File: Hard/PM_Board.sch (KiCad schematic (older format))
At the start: 64 parts, among them J1 Micro_SD_Card_Det_Hirose_DM3AT, J101 LiPo_V+, J102 LiPo_V-, J2 KRC_Conn_SWD, J3 USB_B_Micro, J4 KRC_Conn_CAN, J5 KRC_Conn_CAN, J6 KRC_Conn_CAN, Q1 SSM6J501NU, Q2 2n7002, U1 CY8C58xxLTI-LPxxx, U2 INA226, U3 NCV7342, Y1 24MHz

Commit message: [add] 逆流防止用ダイオードを追加
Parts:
- added D6, D7: RSX101VA, Diode_SMD:D_TUMD2, symbol Device:D_Schottky_Small
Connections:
- net +3V3: now also D7.2 (A)
- net +5V: now also D6.2 (A)
- net at C17.1, C19.1, Q1.4 (S)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: now also D6.1 (K), D7.1 (K)
- no-connect marks 9 -> 36
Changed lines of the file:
@@
 EESchema Schematic File Version 4
 LIBS:PM_Board-cache
-EELAYER 26 0
+EELAYER 30 0
 EELAYER END
 $Descr A4 11693 8268
@@
 P 2900 2950
 F 0 "#PWR0133" H 2900 2700 50  0001 C CNN
-F 1 "GND" H 2905 2777 50  0000 C CNN
+F 1 "GND" H 3050 2900 50  0000 C CNN
 F 2 "" H 2900 2950 50  0001 C CNN
 F 3 "" H 2900 2950 50  0001 C CNN
@@
 U 1 1 5DC30610
 P 2900 4550
-F 0 "VR2" H 2900 4865 50  0000 C CNN
-F 1 "NCP718ASN330T1G" H 2900 4774 50  0000 C CNN
+F 0 "VR2" H 2900 4650 50  0000 C CNN
+F 1 "NCP718ASN330T1G" H 3300 4350 50  0000 C CNN
 F 2 "Package_TO_SOT_SMD:TSOT-23-5" H 2800 4750 50  0001 C CNN
 F 3 "https://www.onsemi.com/pub/Collateral/NCP718-D.PDF" H 2900 4850 50  0001 C CNN
@@
 U 1 1 5DC3080F
 P 2900 3550
-F 0 "VR1" H 2900 3865 50  0000 C CNN
-F 1 "NCP718ASN500T1G" H 2900 3774 50  0000 C CNN
+F 0 "VR1" H 2900 3650 50  0000 C CNN
+F 1 "NCP718ASN500T1G" H 3300 3350 50  0000 C CNN
 F 2 "Package_TO_SOT_SMD:TSOT-23-5" H 2800 3750 50  0001 C CNN
 F 3 "https://www.onsemi.com/pub/Collateral/NCP718-D.PDF" H 2900 3850 50  0001 C CNN
@@
 $EndComp
 Wire Wire Line
-	2400 3500 2550 3500
+	2400 3500 2450 3500
 Wire Wire Line
 	2400 3600 2550 3600
@@
 Connection ~ 2400 4500
 Wire Wire Line
-	2400 4500 2550 4500
-Wire Wire Line
-	3250 4500 3700 4500
-Wire Wire Line
-	3250 3500 3700 3500
+	2400 4500 2450 4500
+Wire Wire Line
+	3250 4500 3350 4500
+Wire Wire Line
+	3250 3500 3350 3500
 Wire Wire Line
 	2900 3800 2900 3900
@@
 Wire Wire Line
 	5050 4100 5350 4100
+$Comp
+L Device:D_Schottky_Small D6
+U 1 1 5D91C8E7
+P 2900 3350
+F 0 "D6" H 2900 3555 50  0000 C CNN
+F 1 "RSX101VA" H 2900 3464 50  0000 C CNN
+F 2 "Diode_SMD:D_TUMD2" V 2900 3350 50  0001 C CNN
+F 3 "http://akizukidenshi.com/download/ds/rohm/rsx101vam30-j.pdf" V 2900 3350 50  0001 C CNN
+F 4 "秋月電子" H 2900 3350 50  0001 C CNN "Agency"
+F 5 "http://akizukidenshi.com/catalog/g/gI-05951/" H 2900 3350 50  0001 C CNN "Link"
+F 6 "RSX101VAM-30TR" H 2900 3350 50  0001 C CNN "MPN"
+	1    2900 3350
+	1    0    0    -1
+$EndComp
+Wire Wire Line
+	2800 3350 2450 3350
+Wire Wire Line
+	2450 3350 2450 3500
+Connection ~ 2450 3500
+Wire Wire Line
+	2450 3500 2550 3500
+Wire Wire Line
+	3000 3350 3350 3350
+Wire Wire Line
+	3350 3350 3350 3500
+Connection ~ 3350 3500
+Wire Wire Line
+	3350 3500 3700 3500
+$Comp
+L Device:D_Schottky_Small D7
+U 1 1 5D94B0D3
+P 2900 4350
+F 0 "D7" H 2900 4555 50  0000 C CNN
+F 1 "RSX101VA" H 2900 4464 50  0000 C CNN
+F 2 "Diode_SMD:D_TUMD2" V 2900 4350 50  0001 C CNN
+F 3 "http://akizukidenshi.com/download/ds/rohm/rsx101vam30-j.pdf" V 2900 4350 50  0001 C CNN
+F 4 "秋月電子" H 2900 4350 50  0001 C CNN "Agency"
+F 5 "http://akizukidenshi.com/catalog/g/gI-05951/" H 2900 4350 50  0001 C CNN "Link"
+F 6 "RSX101VAM-30TR" H 2900 4350 50  0001 C CNN "MPN"
+	1    2900 4350
+	1    0    0    -1
+$EndComp
+Wire Wire Line
+	2800 4350 2450 4350
+Wire Wire Line
+	2450 4350 2450 4500
+Connection ~ 2450 4500
+Wire Wire Line
+	2450 4500 2550 4500
+Wire Wire Line
+	3000 4350 3350 4350
+Wire Wire Line
+	3350 4350 3350 4500
+Connection ~ 3350 4500
+Wire Wire Line
+	3350 4500 3700 4500
+NoConn ~ 5350 3200
+NoConn ~ 5350 3300
+NoConn ~ 5350 3400
+NoConn ~ 5350 3500
+NoConn ~ 5350 4500
+NoConn ~ 5350 4600
+NoConn ~ 5350 4850
+NoConn ~ 5350 4950
+NoConn ~ 5350 5050
+NoConn ~ 5350 5150
+NoConn ~ 5350 5250
+NoConn ~ 8050 2800
+NoConn ~ 8050 2900
+NoConn ~ 8050 3000
+NoConn ~ 8050 3100
+NoConn ~ 8050 3200
+NoConn ~ 8050 3300
+NoConn ~ 8050 3700
+NoConn ~ 8050 3800
+NoConn ~ 8050 3900
+NoConn ~ 8050 4000
+NoConn ~ 8050 4100
+NoConn ~ 8050 4200
+NoConn ~ 8050 4300
+NoConn ~ 8050 4400
+NoConn ~ 8050 5200
+NoConn ~ 8050 5300
 $EndSCHEMATC

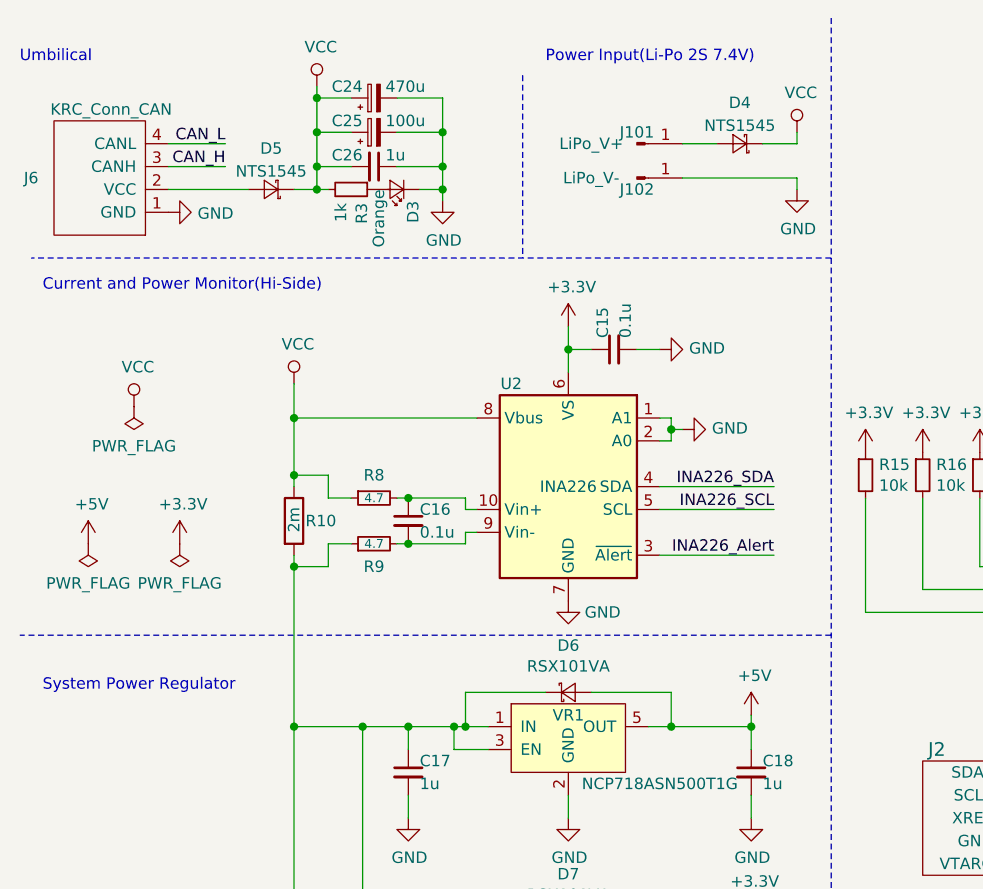
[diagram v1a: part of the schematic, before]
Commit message: [update] パターンを編集完了
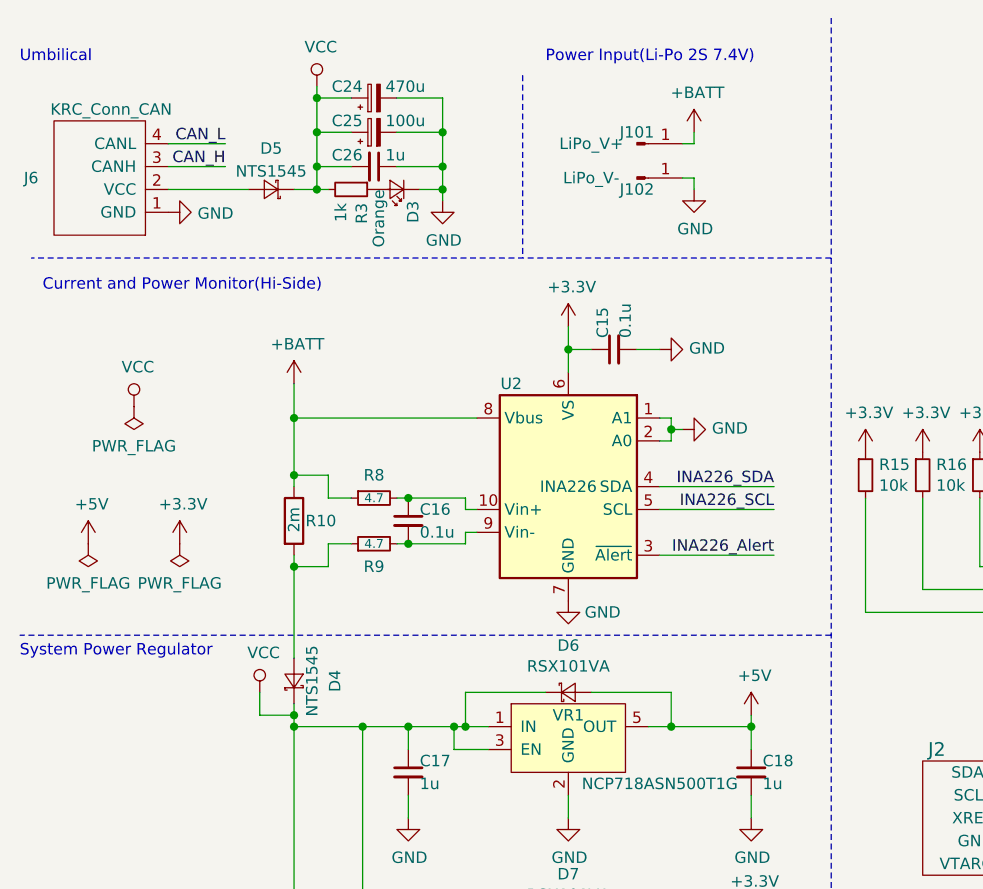
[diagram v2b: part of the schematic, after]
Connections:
- net VCC: now also C17.1, C19.1, D6.1 (K), D7.1 (K), Q1.4 (S), Q1.8, R13.1, VR1.1 (IN), VR1.3 (EN), VR2.1 (IN), VR2.3 (EN); no longer R10.1, R8.1, U2.8 (Vbus)
- net at D4.2 (A): now also R10.2, R9.1; no longer J101.1 (Pin_1)
- new net +BATT: J101.1 (Pin_1), R10.1, R8.1, U2.8 (Vbus)
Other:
- moved on the sheet: D4
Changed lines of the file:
@@
 L power:GND #PWR0134
 U 1 1 5DCE33BD
-P 3900 1150
-F 0 "#PWR0134" H 3900 900 50  0001 C CNN
-F 1 "GND" H 3905 977 50  0000 C CNN
-F 2 "" H 3900 1150 50  0001 C CNN
-F 3 "" H 3900 1150 50  0001 C CNN
-	1    3900 1150
+P 3450 1150
+F 0 "#PWR0134" H 3450 900 50  0001 C CNN
+F 1 "GND" H 3455 977 50  0000 C CNN
+F 2 "" H 3450 1150 50  0001 C CNN
+F 3 "" H 3450 1150 50  0001 C CNN
+	1    3450 1150
 	1    0    0    -1
 $EndComp
@@
 Text Notes 600  1600 0    50   ~ 0
 Current and Power Monitor(Hi-Side)
-Text Notes 600  3350 0    50   ~ 0
+Text Notes 500  3200 0    50   ~ 0
 System Power Regulator
 Text Notes 750  5350 0    50   ~ 0
@@
 	0    -1   1    0
 $EndComp
-$Comp
-L power:VCC #PWR0141
-U 1 1 5DAE3A9E
-P 3900 900
-F 0 "#PWR0141" H 3900 750 50  0001 C CNN
-F 1 "VCC" H 3917 1073 50  0000 C CNN
-F 2 "" H 3900 900 50  0001 C CNN
-F 3 "" H 3900 900 50  0001 C CNN
-	1    3900 900
-	1    0    0    -1
-$EndComp
-Wire Wire Line
-	3900 900  3900 950
-$Comp
-L power:VCC #PWR0142
-U 1 1 5DB04A5B
-P 1700 2000
-F 0 "#PWR0142" H 1700 1850 50  0001 C CNN
-F 1 "VCC" H 1717 2173 50  0000 C CNN
-F 2 "" H 1700 2000 50  0001 C CNN
-F 3 "" H 1700 2000 50  0001 C CNN
-	1    1700 2000
-	1    0    0    -1
-$EndComp
 Wire Wire Line
 	1700 2000 1700 2150
@@
 L Device:D_Schottky_Small D4
 U 1 1 5DD308E3
-P 3650 950
-F 0 "D4" H 3650 800 50  0000 C TNN
-F 1 "NTS1545" H 3650 900 50  0000 C TNN
-F 2 "KUTKiCad_footprint:DFN5_5x6_1.27P" H 3650 950 50  0001 C CNN
-F 3 "https://www.onsemi.com/pub/Collateral/NTS1545MFS-D.PDF" H 3650 950 50  0001 C CNN
-F 4 "Digikey" H 3650 950 50  0001 C CNN "Agency"
-F 5 "NTS1545MFST1G" H 3650 950 50  0001 C CNN "MPN"
-F 6 "https://www.digikey.jp/product-detail/ja/on-semiconductor/NTS1545MFST1G/NTS1545MFST1GOSCT-ND/5022596" H 3650 950 50  0001 C CNN "Link"
-	1    3650 950
-	-1   0    0    1
+P 1700 3300
+F 0 "D4" H 1700 3150 50  0000 C TNN
+F 1 "NTS1545" H 1700 3250 50  0000 C TNN
+F 2 "KUTKiCad_footprint:DFN5_5x6_1.27P" H 1700 3300 50  0001 C CNN
+F 3 "https://www.onsemi.com/pub/Collateral/NTS1545MFS-D.PDF" H 1700 3300 50  0001 C CNN
+F 4 "Digikey" H 1700 3300 50  0001 C CNN "Agency"
+F 5 "NTS1545MFST1G" H 1700 3300 50  0001 C CNN "MPN"
+F 6 "https://www.digikey.jp/product-detail/ja/on-semiconductor/NTS1545MFST1G/NTS1545MFST1GOSCT-ND/5022596" H 1700 3300 50  0001 C CNN "Link"
+	1    1700 3300
+	0    -1   -1   0
 $EndComp
 $Comp
@@
 	8750 3500 8750 3600
 Wire Wire Line
-	1700 2800 1700 3500
-Connection ~ 1700 2800
-Wire Wire Line
 	1400 950  1150 950
 Wire Wire Line
-	3750 950  3900 950
-Wire Wire Line
-	3900 1150 3900 1100
+	3450 1150 3450 1100
 $Comp
 L Device:LED_Small D3
@@
 Wire Wire Line
 	2350 1150 2350 1200
-Wire Wire Line
-	3550 950  3400 950
-Wire Wire Line
-	3900 1100 3400 1100
 $Comp
 L Device:R_Small R15
@@
 Wire Wire Line
 	2850 5650 3250 5650
-Wire Wire Line
-	1700 3500 1700 5150
-Connection ~ 1700 3500
 Wire Wire Line
 	1700 5850 1700 6150
@@
 NoConn ~ 8050 5200
 NoConn ~ 8050 5300
+$Comp
+L power:+BATT #PWR0141
+U 1 1 5DC0E776
+P 3450 900
+F 0 "#PWR0141" H 3450 750 50  0001 C CNN
+F 1 "+BATT" H 3465 1073 50  0000 C CNN
+F 2 "" H 3450 900 50  0001 C CNN
+F 3 "" H 3450 900 50  0001 C CNN
+	1    3450 900
+	1    0    0    -1
+$EndComp
+Wire Wire Line
+	3450 900  3450 950
+Wire Wire Line
+	3450 950  3400 950
+$Comp
+L power:+BATT #PWR0142
+U 1 1 5DC26E97
+P 1700 2000
+F 0 "#PWR0142" H 1700 1850 50  0001 C CNN
+F 1 "+BATT" H 1715 2173 50  0000 C CNN
+F 2 "" H 1700 2000 50  0001 C CNN
+F 3 "" H 1700 2000 50  0001 C CNN
+	1    1700 2000
+	1    0    0    -1
+$EndComp
+Wire Wire Line
+	1700 2800 1700 3200
+Connection ~ 1700 2800
+Wire Wire Line
+	1700 3400 1700 3450
+Connection ~ 1700 3500
+Wire Wire Line
+	3450 1100 3400 1100
+Wire Wire Line
+	1700 3500 1700 5150
+$Comp
+L power:VCC #PWR0151
+U 1 1 5DD8F5B1
+P 1550 3350
+F 0 "#PWR0151" H 1550 3200 50  0001 C CNN
+F 1 "VCC" H 1567 3523 50  0000 C CNN
+F 2 "" H 1550 3350 50  0001 C CNN
+F 3 "" H 1550 3350 50  0001 C CNN
+	1    1550 3350
+	1    0    0    -1
+$EndComp
+Wire Wire Line
+	1550 3350 1550 3450
+Wire Wire Line
+	1550 3450 1700 3450
+Connection ~ 1700 3450
+Wire Wire Line
+	1700 3450 1700 3500
 $EndSCHEMATC

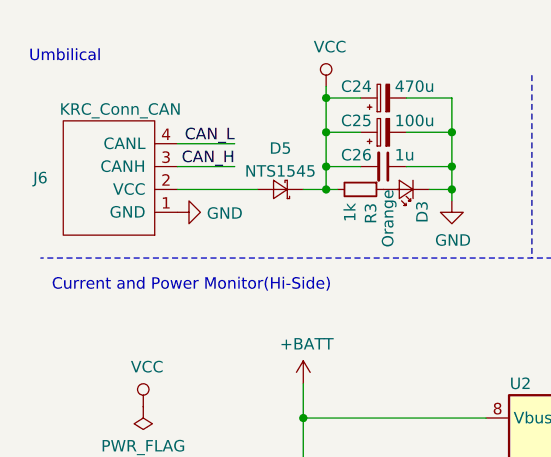
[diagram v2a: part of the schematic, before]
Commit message: [update] アンビリカルをDF1Eに変更
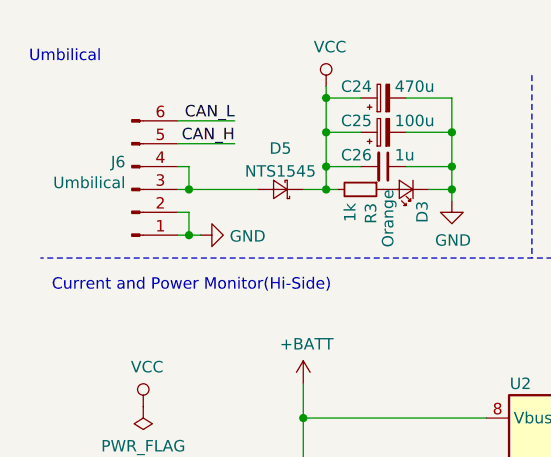
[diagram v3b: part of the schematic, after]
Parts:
- removed J6: KRC_Conn_CAN, KUTKiCad_footprint:Hirose_DF33-DF33C-4DP-3.3DSA_2x02_P3.3_Vertical, symbol KUTKiCad_symbol:KRC_Conn_CAN
- added J6: Umbilical, KUTKiCad_footprint:Hirose_DF1E_DF1E-6P-2.5DS_1x06_P2.5mm_Vertical, symbol Connector:Conn_01x06_Male
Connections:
- net CAN_H: now also J6.5 (Pin_5)
- net CAN_L: now also J6.6 (Pin_6)
- net GND: now also J6.1 (Pin_1), J6.2 (Pin_2)
- net at D5.2 (A): now also J6.3 (Pin_3), J6.4 (Pin_4)
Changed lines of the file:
@@
 EESchema Schematic File Version 4
 LIBS:PM_Board-cache
-EELAYER 30 0
+EELAYER 26 0
 EELAYER END
 $Descr A4 11693 8268
@@
 microSD
 Connection ~ 2000 3500
-$Comp
-L KUTKiCad_symbol:KRC_Conn_CAN J6
-U 1 1 5D97F500
-P 1050 1100
-F 0 "J6" H 1550 1100 50  0000 C CNN
-F 1 "KRC_Conn_CAN" H 1200 800 50  0000 C CNN
-F 2 "KUTKiCad_footprint:Hirose_DF33-DF33C-4DP-3.3DSA_2x02_P3.3_Vertical" H 1050 1100 50  0001 C CNN
-F 3 "https://www.hirose.com/product/document?clcode=&productname=&series=DF33C&documenttype=Catalog&lang=ja&documentid=D51103_ja" H 1050 1100 50  0001 C CNN
-F 4 "Digikey" H 1050 1100 50  0001 C CNN "Agency"
-F 5 "DF33C-4DP-3.3DSA(24)" H 1050 1100 50  0001 C CNN "MPN"
-F 6 "https://www.digikey.jp/products/ja?keywords=DF33C-4DP-3.3DSA(24)" H 0   0   50  0001 C CNN "Link"
-	1    1050 1100
-	-1   0    0    1
-$EndComp
 Text Label 1750 7000 2    50   ~ 0
 CAN_H
 Text Label 1750 7100 2    50   ~ 0
 CAN_L
-Text Label 1400 1050 2    50   ~ 0
+Text Label 1400 950  2    50   ~ 0
 CAN_H
-Text Label 1400 950  2    50   ~ 0
+Text Label 1400 850  2    50   ~ 0
 CAN_L
 Wire Wire Line
-	1400 1050 1150 1050
+	1400 950  1150 950
 $Comp
 L power:GND #PWR0140
 U 1 1 5DA52B7A
-P 1150 1250
-F 0 "#PWR0140" H 1150 1000 50  0001 C CNN
-F 1 "GND" V 1155 1122 50  0000 R CNN
-F 2 "" H 1150 1250 50  0001 C CNN
-F 3 "" H 1150 1250 50  0001 C CNN
-	1    1150 1250
+P 1250 1350
+F 0 "#PWR0140" H 1250 1100 50  0001 C CNN
+F 1 "GND" V 1255 1222 50  0000 R CNN
+F 2 "" H 1250 1350 50  0001 C CNN
+F 3 "" H 1250 1350 50  0001 C CNN
+	1    1250 1350
 	0    -1   1    0
 $EndComp
@@
 	8750 3500 8750 3600
 Wire Wire Line
-	1400 950  1150 950
+	1400 850  1150 850
 Wire Wire Line
 	3450 1150 3450 1100
@@
 Connection ~ 1800 1150
 Wire Wire Line
-	1500 1150 1150 1150
+	1500 1150 1200 1150
 $Comp
 L KUTKiCad_symbol:SSM6J501NU Q1
@@
 Wire Wire Line
 	1700 3450 1700 3500
+$Comp
+L Connector:Conn_01x06_Male J6
+U 1 1 5D968A87
+P 950 1150
+F 0 "J6" H 922 1030 50  0000 R CNN
+F 1 "Umbilical" H 922 1121 50  0000 R CNN
+F 2 "KUTKiCad_footprint:Hirose_DF1E_DF1E-6P-2.5DS_1x06_P2.5mm_Vertical" H 950 1150 50  0001 C CNN
+F 3 "https://www.hirose.com/product/document?clcode=&productname=&series=DF1E&documenttype=Catalog&lang=ja&documentid=D49651_ja" H 950 1150 50  0001 C CNN
+F 4 "Digikey" H 950 1150 50  0001 C CNN "Agency"
+F 5 "DF1EC-6P-2.5DSA(35)" H 950 1150 50  0001 C CNN "MPN"
+F 6 "https://www.digikey.jp/product-detail/ja/hirose-electric-co-ltd/DF1EC-6P-2.5DSA-35/H125168-ND/5416404" H 950 1150 50  0001 C CNN "Link"
+	1    950  1150
+	1    0    0    1
+$EndComp
+Wire Wire Line
+	1150 1250 1200 1250
+Wire Wire Line
+	1200 1250 1200 1350
+Wire Wire Line
+	1150 1350 1200 1350
+Connection ~ 1200 1350
+Wire Wire Line
+	1200 1350 1250 1350
+Wire Wire Line
+	1150 1050 1200 1050
+Wire Wire Line
+	1200 1050 1200 1150
+Connection ~ 1200 1150
+Wire Wire Line
+	1200 1150 1150 1150
 $EndSCHEMATC
